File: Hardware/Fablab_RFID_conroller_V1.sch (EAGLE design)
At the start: 46 parts, among them IC1 V_REG_LDOSMD, J1 JACK-DC-3P-3410020P1

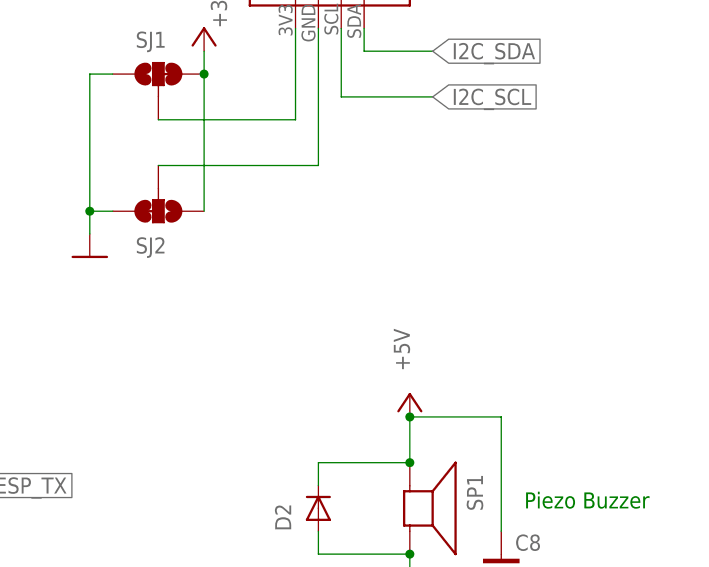
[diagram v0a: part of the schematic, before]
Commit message: updated schematic with errata
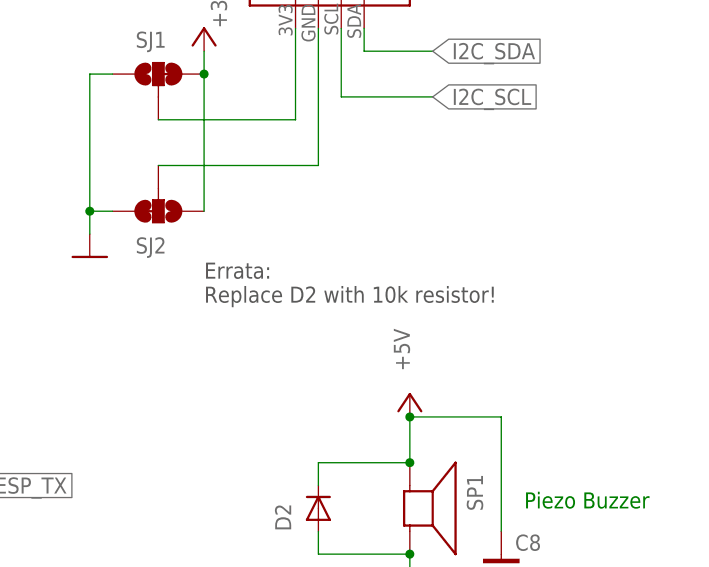
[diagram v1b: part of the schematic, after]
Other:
- note added: "Errata: Replace D2 with 10k resistor!"
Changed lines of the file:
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@@
 reversed, use solder
 jumpers to switch</text>
+<text x="332.74" y="81.28" size="1.778" layer="92">Errata:
+Replace D2 with 10k resistor!</text>
 </plain>
 <instances>

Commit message: bugfixes & cosmetics
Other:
- note added: "Errata: Missing connection-> use jumperwire"
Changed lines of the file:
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@@
 <text x="332.74" y="81.28" size="1.778" layer="92">Errata:
 Replace D2 with 10k resistor!</text>
+<text x="226.06" y="236.22" size="1.778" layer="92">Errata:
+Missing connection-&gt; use jumperwire</text>
 </plain>
 <instances>
@@
 </segment>
 <segment>
-<wire x1="266.7" y1="236.22" x2="266.7" y2="238.76" width="0.1524" layer="91"/>
-<pinref part="P+6" gate="1" pin="+5V"/>
-</segment>
-<segment>

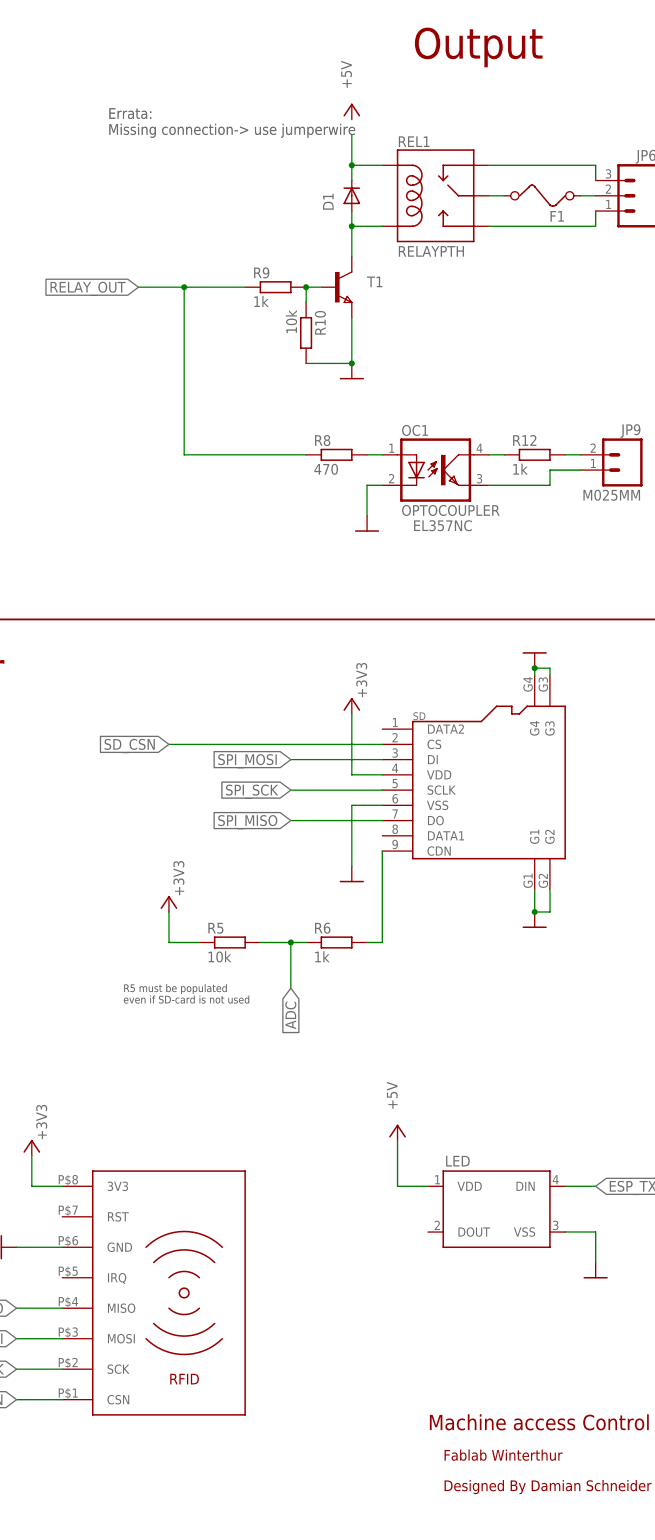
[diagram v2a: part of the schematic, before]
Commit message: Address erratum: Fix +5V connection of relay coil.
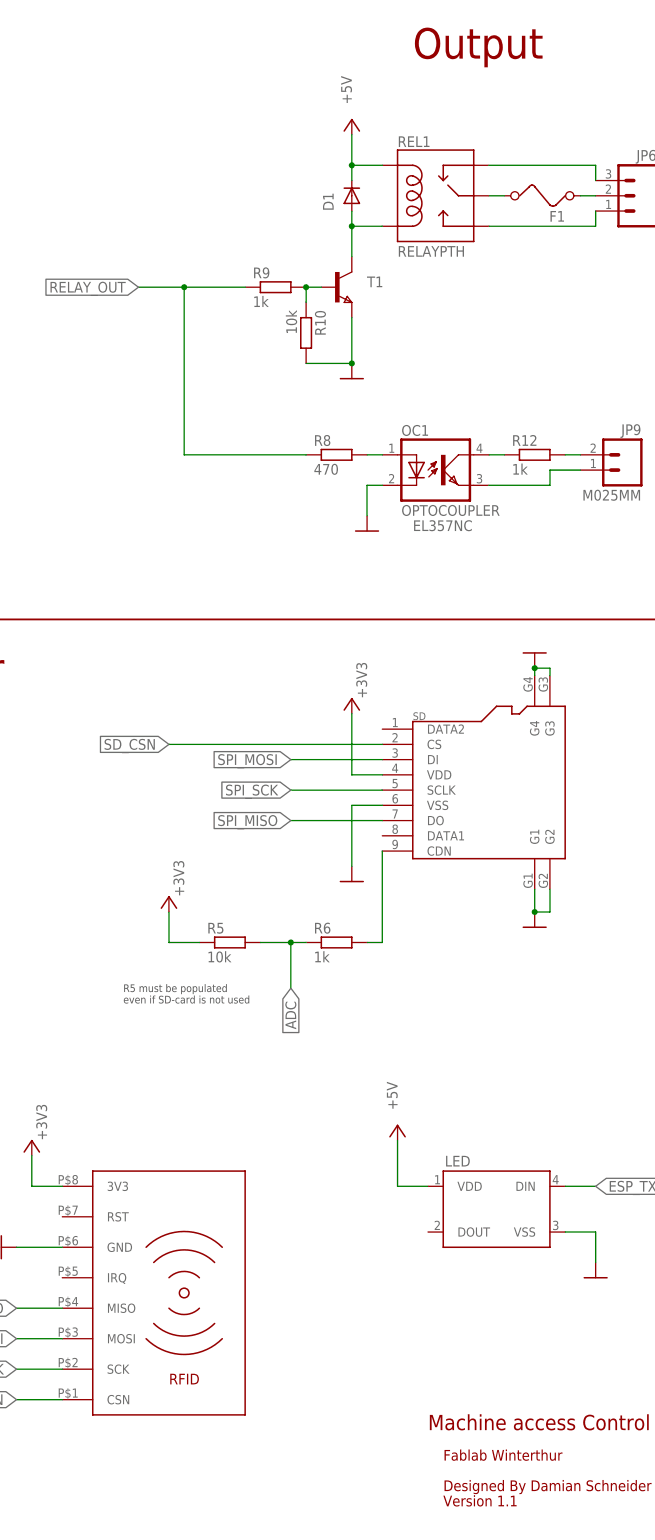
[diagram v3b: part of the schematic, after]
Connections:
- removed net N$10: D1.C, REL1.COIL1
- net +5V: now also D1.C, REL1.COIL1
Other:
- note added: "Version 1.1"
- note removed: "Errata: Missing connection-> use jumperwire"
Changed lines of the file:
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@@
 <text x="332.74" y="81.28" size="1.778" layer="92">Errata:
 Replace D2 with 10k resistor!</text>
-<text x="226.06" y="236.22" size="1.778" layer="92">Errata:
-Missing connection-&gt; use jumperwire</text>
+<text x="281.94" y="7.62" size="1.778" layer="94">Version 1.1</text>
 </plain>
 <instances>
@@
 <instance part="R9" gate="G$1" x="254" y="210.82"/>
 <instance part="R10" gate="G$1" x="259.08" y="203.2" rot="R270"/>
-<instance part="P+6" gate="1" x="266.7" y="241.3" smashed="yes">
-<attribute name="VALUE" x="266.7" y="243.84" size="1.778" layer="96" rot="R90"/>
+<instance part="P+6" gate="1" x="266.7" y="238.76" smashed="yes">
+<attribute name="VALUE" x="266.7" y="241.3" size="1.778" layer="96" rot="R90"/>
 </instance>
 <instance part="D1" gate="G$1" x="266.7" y="226.06" smashed="yes" rot="R90">
@@
 <pinref part="P+2" gate="1" pin="+5V"/>
 <wire x1="96.52" y1="210.82" x2="96.52" y2="213.36" width="0.1524" layer="91"/>
+</segment>
+<segment>
+<pinref part="D1" gate="G$1" pin="C"/>
+<wire x1="266.7" y1="228.6" x2="266.7" y2="231.14" width="0.1524" layer="91"/>
+<pinref part="REL1" gate="G$1" pin="COIL1"/>
+<wire x1="266.7" y1="231.14" x2="266.7" y2="236.22" width="0.1524" layer="91"/>
+<wire x1="271.78" y1="231.14" x2="266.7" y2="231.14" width="0.1524" layer="91"/>
+<junction x="266.7" y="231.14"/>
+<pinref part="P+6" gate="1" pin="+5V"/>
 </segment>
 </net>
@@
 </segment>
 </net>
-<net name="N$10" class="0">
-<segment>
-<pinref part="D1" gate="G$1" pin="C"/>
-<wire x1="266.7" y1="228.6" x2="266.7" y2="231.14" width="0.1524" layer="91"/>
-<pinref part="REL1" gate="G$1" pin="COIL1"/>
-<wire x1="266.7" y1="231.14" x2="266.7" y2="236.22" width="0.1524" layer="91"/>
-<wire x1="271.78" y1="231.14" x2="266.7" y2="231.14" width="0.1524" layer="91"/>
-<junction x="266.7" y="231.14"/>
-</segment>
-</net>

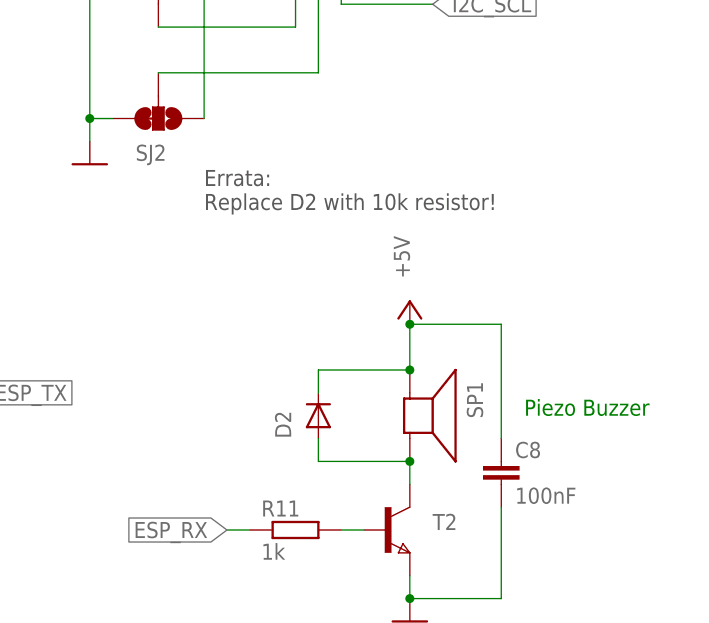
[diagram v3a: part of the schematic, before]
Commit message: Address erratum: Replace diode D2 by 10k resistor R13.
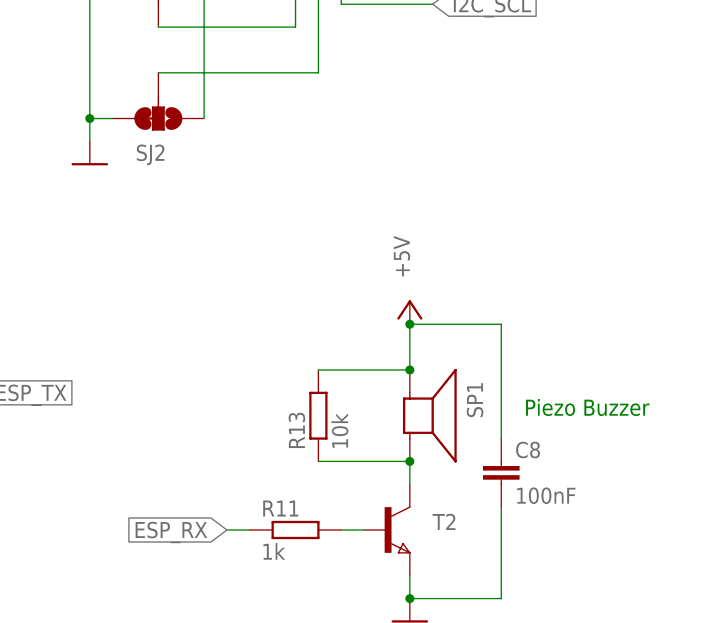
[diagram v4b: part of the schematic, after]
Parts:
- removed D2: (no value), diode:DIODE-MINIMELF
- added R13: 10k, resistor:R-EU_R0603
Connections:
- net +5V: now also R13.2; no longer D2.C
- net N$8: now also R13.1; no longer D2.A
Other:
- note removed: "Errata: Replace D2 with 10k resistor!"
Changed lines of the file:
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@@
 <part name="T2" library="zetex" deviceset="NPNSOT23" device=""/>
 <part name="R11" library="resistor" deviceset="R-EU_" device="R0603" value="1k"/>
-<part name="D2" library="diode" deviceset="DIODE-" device="MINIMELF"/>
 <part name="P+7" library="supply1" deviceset="+5V" device=""/>
 <part name="C8" library="resistor" deviceset="C-EU" device="C0603" value="100nF"/>
@@
 <part name="SJ2" library="SparkFun-Passives" deviceset="JUMPER-PAD-3-2OF3_NC_BY_TRACE" device="_LARGE"/>
 <part name="+3V6" library="supply1" deviceset="+3V3" device=""/>
+<part name="R13" library="resistor" deviceset="R-EU_" device="R0603" value="10k"/>
 </parts>
 <sheets>
@@
 reversed, use solder
 jumpers to switch</text>
-<text x="332.74" y="81.28" size="1.778" layer="92">Errata:
-Replace D2 with 10k resistor!</text>
 <text x="281.94" y="7.62" size="1.778" layer="94">Version 1.1</text>
 </plain>
@@
 </instance>
 <instance part="R11" gate="G$1" x="342.9" y="45.72"/>
-<instance part="D2" gate="G$1" x="345.44" y="58.42" smashed="yes" rot="R90">
-<attribute name="NAME" x="342.4174" y="55.88" size="1.778" layer="95" rot="R90"/>
-<attribute name="VALUE" x="347.7514" y="60.96" size="1.778" layer="96" rot="R90"/>
-</instance>
 <instance part="P+7" gate="1" x="355.6" y="71.12" smashed="yes">
 <attribute name="VALUE" x="355.6" y="73.66" size="1.778" layer="96" rot="R90"/>
@@
 <attribute name="VALUE" x="335.28" y="111.76" size="1.778" layer="96" rot="R90"/>
 </instance>
+<instance part="R13" gate="G$1" x="345.44" y="58.42" rot="R90"/>
 </instances>
 <busses>
@@
 </segment>
 <segment>
-<pinref part="D2" gate="G$1" pin="C"/>
 <pinref part="SP1" gate="S1" pin="+"/>
-<wire x1="345.44" y1="60.96" x2="345.44" y2="63.5" width="0.1524" layer="91"/>
 <wire x1="345.44" y1="63.5" x2="355.6" y2="63.5" width="0.1524" layer="91"/>
 <wire x1="355.6" y1="63.5" x2="355.6" y2="68.58" width="0.1524" layer="91"/>
@@
 <wire x1="365.76" y1="68.58" x2="355.6" y2="68.58" width="0.1524" layer="91"/>
 <junction x="355.6" y="68.58"/>
+<pinref part="R13" gate="G$1" pin="2"/>
 </segment>
 <segment>
@@
 <wire x1="355.6" y1="53.34" x2="345.44" y2="53.34" width="0.1524" layer="91"/>
 <junction x="355.6" y="53.34"/>
-<pinref part="D2" gate="G$1" pin="A"/>
-<wire x1="345.44" y1="53.34" x2="345.44" y2="55.88" width="0.1524" layer="91"/>
-</segment>
-</net>
+<pinref part="R13" gate="G$1" pin="1"/>
+</segment>
+</net>
